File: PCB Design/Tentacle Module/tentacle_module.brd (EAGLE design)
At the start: 94 x 50.8 mm, 53 parts, among them IC1 5V, T1 NTD5867NL, T2 NTD5867NL, T3 NTD5867NL, T4 NTD5867NL, X3 RJ45-8X, X4 RJ45-8X

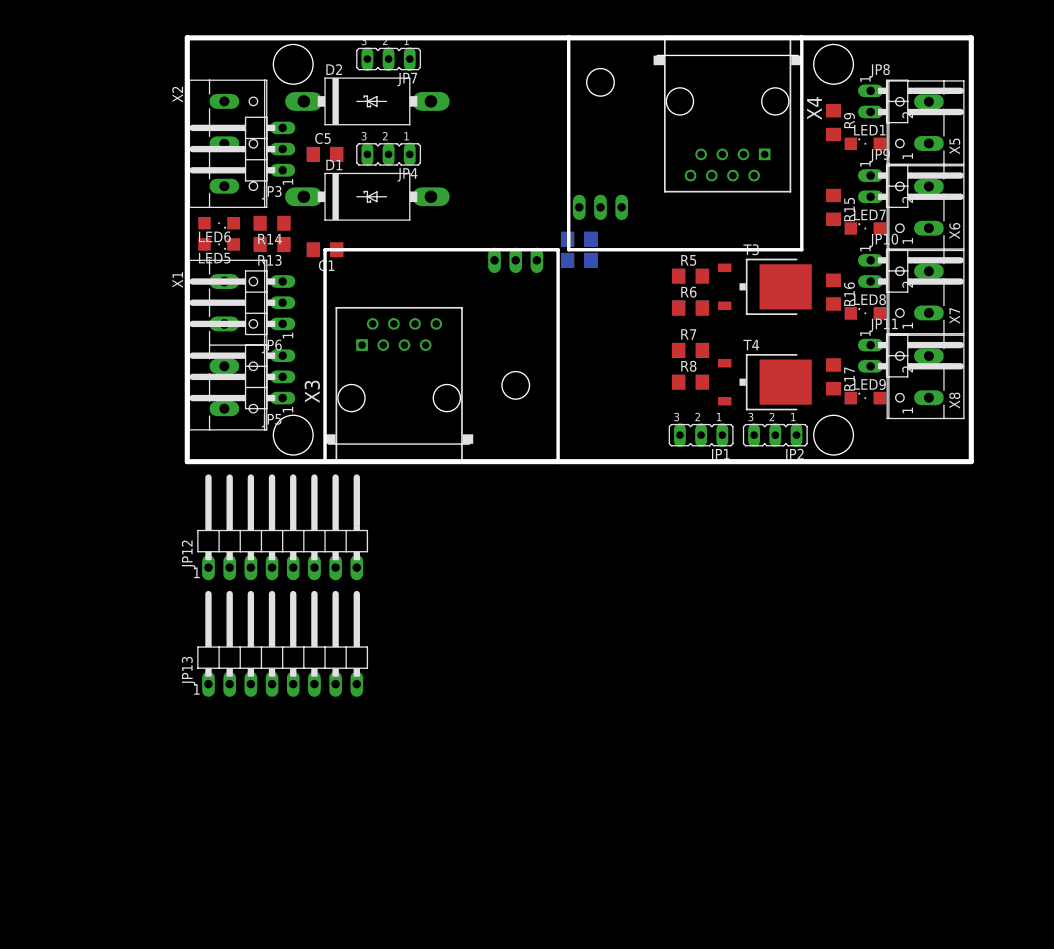
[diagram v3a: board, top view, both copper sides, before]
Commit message: Moved the location of the header
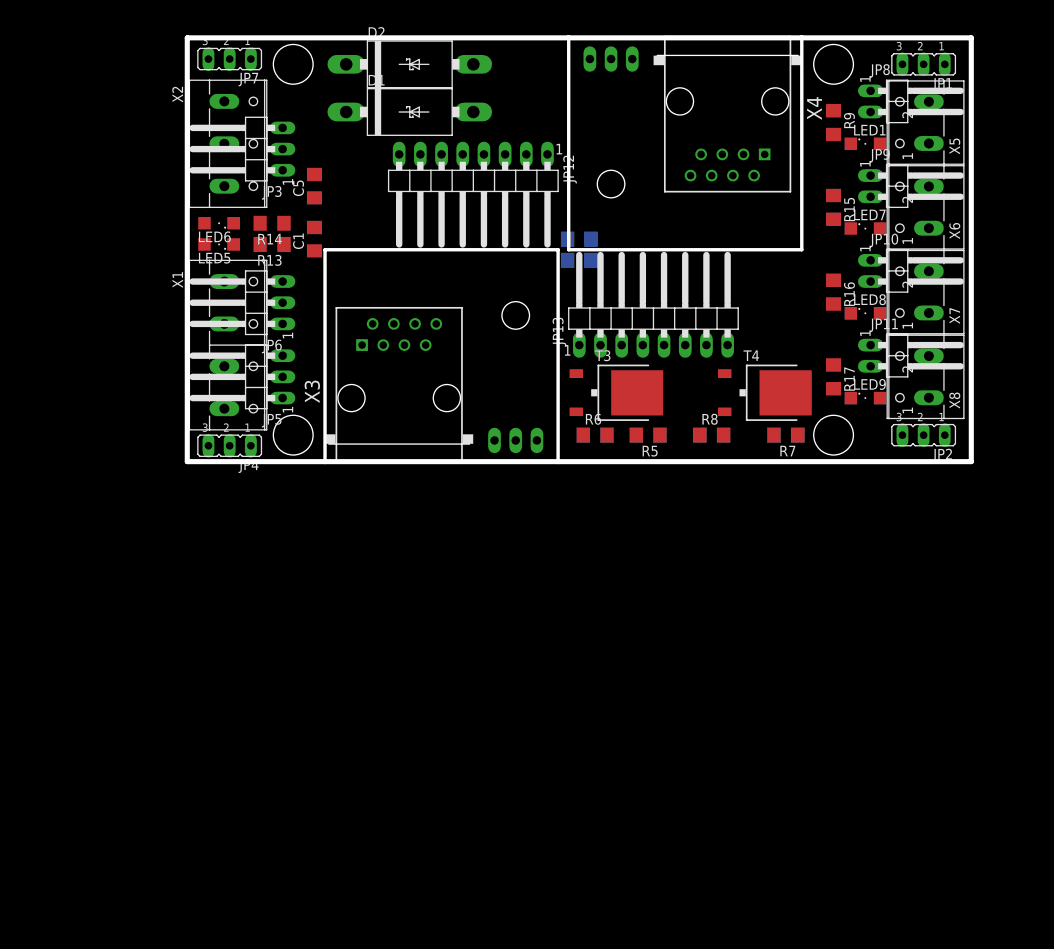
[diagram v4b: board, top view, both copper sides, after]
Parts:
- moved JP13 60.2 mm to (55.9, 17.8)
- moved JP1 51.8 mm to (88.3, 47.6)
- moved JP12 47.7 mm to (34.3, 33.0), turned to 180 degrees
- moved JP4 39.8 mm to (5.08, 1.91)
- moved R3 22.2 mm to (48.9, 3.17)
- moved T1 21.8 mm to (51.4, 8.26)
- moved T3 21.8 mm to (51.4, 8.26)
- moved R5 19.7 mm to (55.2, 3.17), turned to 180 degrees
- moved JP7 19.0 mm to (5.08, 48.3)
- moved R6 19.0 mm to (48.9, 3.17)
- moved JP2 17.8 mm to (88.3, 3.17)
- moved R1 16.1 mm to (55.2, 3.17)
- moved R7 15.3 mm to (71.8, 3.17), turned to 180 degrees
- moved IC1 14.0 mm to (39.4, 6.35), turned to 0 degrees
- moved R2 13.1 mm to (71.8, 3.17)
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
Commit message: Updated the Tentacle module schematic
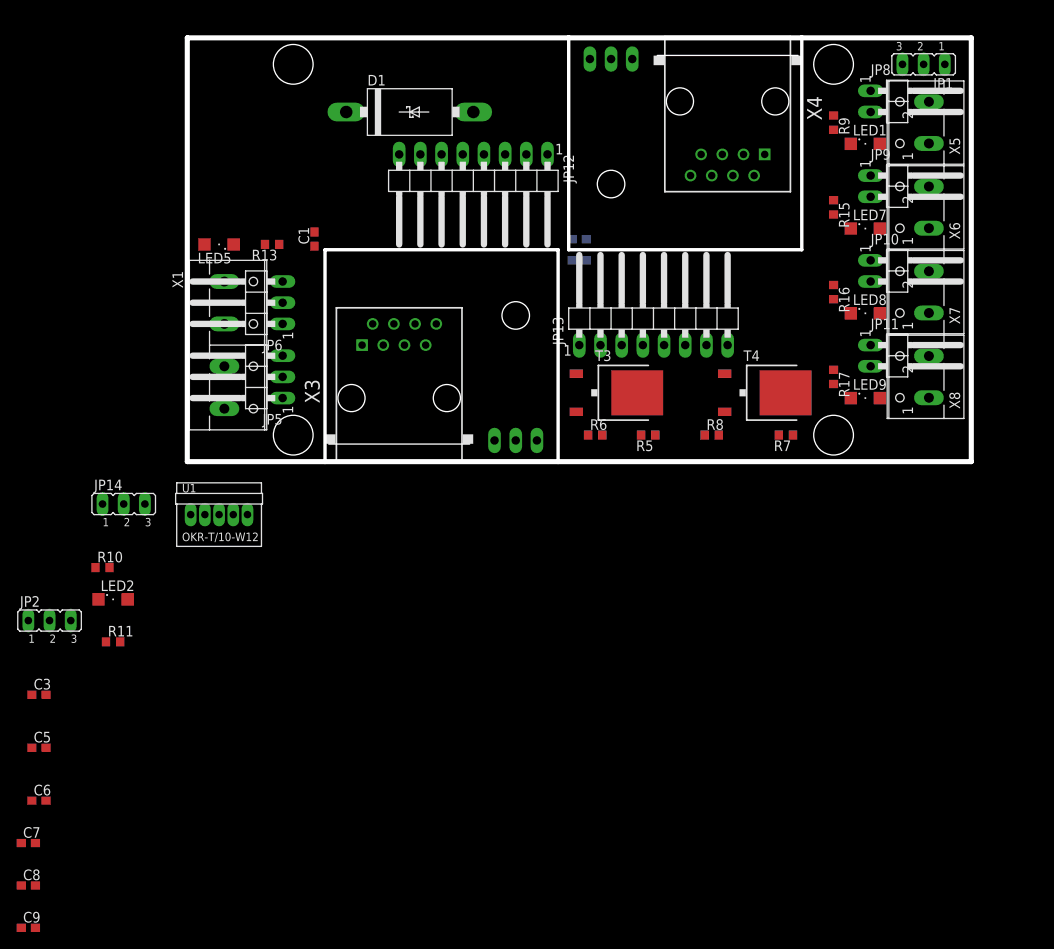
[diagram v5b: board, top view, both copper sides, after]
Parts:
- removed D2: SB540E-G, CBLA_Test_bed_Library:DO201T15
- removed JP3: (no value), CBLA_Test_bed_Library:1X03/90
- removed JP4, JP7: (no value), jumper:JP2
- removed LED6: (no value), led:SML1206
- removed R14: 470, rcl:R1206
- removed X2: (no value), con-wago-508:W237-133
- added C3, C6, C7, C8, C9: 100nF, rcl:C0603
- added JP14: (no value), jumper:JP2
- added LED2: (no value), led:SML1206
- added R10: 267, CBLA_Test_bed_Library:R0603
- added R11: 470, CBLA_Test_bed_Library:R0603
- added U1: OKR-T/10-W12, CBLA_Test_bed_Library:OKR-C90
- C1, C2, C4: device rcl:C1206 -> rcl:C0603
- C5: value 10uF -> 100nF; device rcl:C1206 -> rcl:C0603
- R1, R13, R15, R16, R17, R2, R3, R4, R5, R6, R7, R8, R9: device rcl:R1206 -> CBLA_Test_bed_Library:R0603
- moved JP2 107.1 mm to (-16.5, -19.1), turned to 0 degrees
- moved C5 75.0 mm to (-17.8, -34.3), turned to 0 degrees
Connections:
- removed net +12V1: JP7.2
- removed net +5V_SW-REG: C5.1, D2.C, JP3.1, JP3.3, X2.1, X2.3
- removed net GND1: R14.1
- removed net N$11: JP4.3, LED5.A
- removed net N$12: LED6.C, R14.2
- removed net N$13: JP7.3, LED6.A
- new net 5V_ENABLE: JP14.2, U1.ON/OFF
- new net N$6: R10.2, U1.TRIM
- new net N$7: LED2.C, R11.2
- new net PWR_LED_GND: D1.A, JP2.1, R11.1, R13.1, X1.2
- net +12V: now also JP14.3, LED5.A, U1.VIN, X1.4; no longer JP4.2
- net +3V3: now also C5.1
- net +5V: now also C3.1; no longer JP2.1, JP2.3
- net +5V_HI-PWR: now also C6.1, C7.1, C8.1, C9.1, LED2.A, U1.VOUT; no longer JP2.2
- net GND: now also C3.2, C6.2, C7.2, C8.2, C9.2, JP14.1, JP2.2, R10.1, U1.GND; no longer D1.A, D2.A, JP3.2, R13.1, X1.2, X2.2

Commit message: Preliminary part placement for the tentacle board
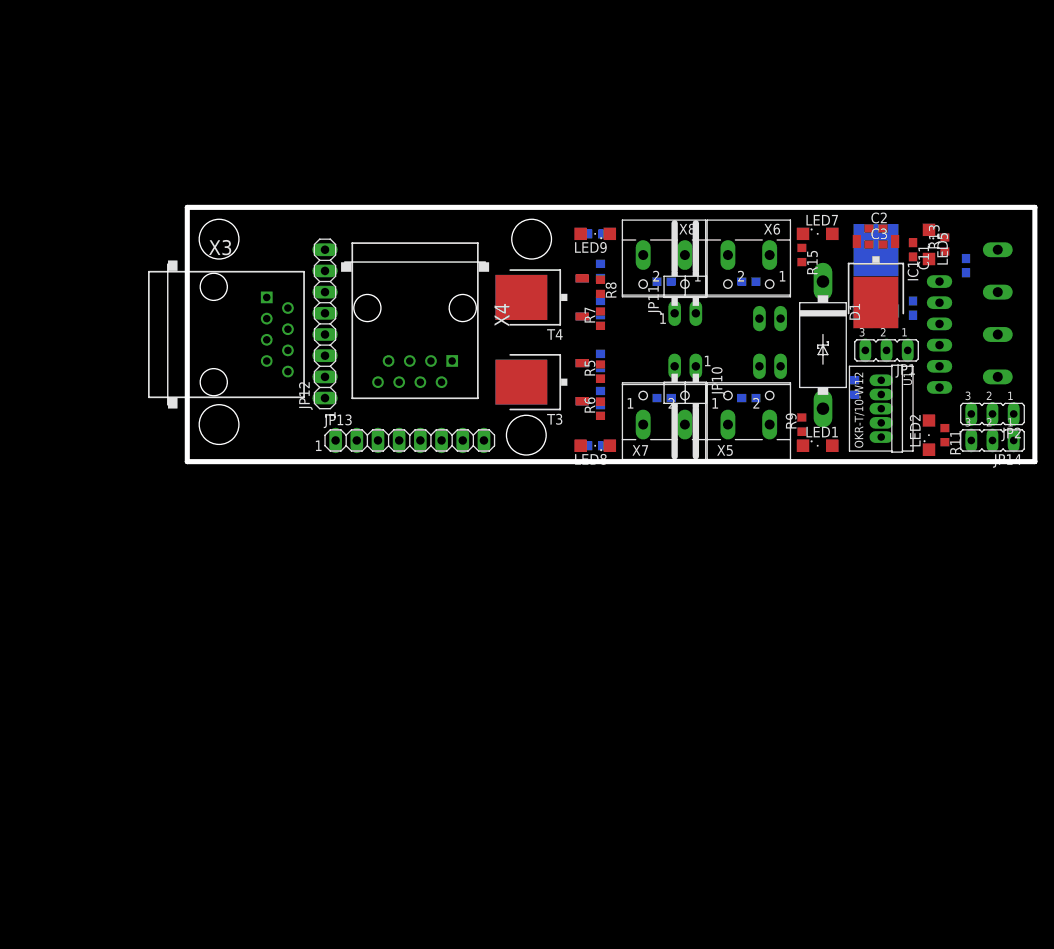
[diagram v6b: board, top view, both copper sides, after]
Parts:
- removed IC2: (no value), CBLA_Test_bed_Library:TO220L1
- added C10, C11: 10uF, rcl:C0603
- added IC3: 3.3V, CBLA_Test_bed_Library:DPACK
- IC1: value 5V -> 5.0V; device CBLA_Test_bed_Library:TO220L1 -> CBLA_Test_bed_Library:DPACK
- JP12, JP13: device CBLA_Test_bed_Library:1X08/90 -> CBLA_Test_bed_Library:1X08
- moved JP2 115.7 mm to (96.5, 5.71), turned to 180 degrees
- moved C3 113.9 mm to (82.5, 26.0)
- moved C5 113.3 mm to (82.5, 18.4), flipped to the bottom, turned to 180 degrees
- moved C7 109.5 mm to (67.3, 21.6), flipped to the bottom, turned to 180 degrees
- moved C9 108.7 mm to (57.1, 21.6), flipped to the bottom, turned to 180 degrees
- moved JP14 104.4 mm to (96.5, 2.54), turned to 180 degrees
- moved R11 102.7 mm to (90.8, 3.17), turned to 270 degrees
- moved LED2 99.8 mm to (88.9, 3.17), turned to 90 degrees
- moved C6 97.8 mm to (67.3, 7.62), flipped to the bottom
- moved C8 96.0 mm to (57.1, 7.62), flipped to the bottom
- moved R10 92.7 mm to (80.0, 8.89), flipped to the bottom, turned to 270 degrees
- moved X1 91.5 mm to (96.5, 17.8), flipped to the bottom
- moved JP5 86.8 mm to (94.0, 19.1), flipped to the bottom
- moved JP6 86.7 mm to (94.0, 11.4), flipped to the bottom
- moved LED5 85.1 mm to (88.9, 26.0), turned to 270 degrees
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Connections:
- removed net N$15: LED8.C, R16.2
- removed net N$16: LED9.C, R17.2
- new net N$12: LED7.A, R15.1
- new net N$13: LED8.A, R16.1
- net +12V: now also C10.1, C11.1, IC3.1; no longer IC2.1
- net +3V3: now also IC3.3; no longer IC2.3
- net +5V: no longer JP1.2
- net +5V_HI-PWR: now also JP1.2
- net GND: now also C10.2, C11.2, IC3.2; no longer IC2.2
- net N$14: now also LED9.A, R17.1; no longer LED7.C, R15.2
- net N$5: now also LED1.A, R9.1; no longer LED1.C, R9.2
- net PWR_LED_GND: now also JP2.3; no longer JP2.1
- net SMA1_OUT-: now also LED1.C; no longer R9.1
- net SMA2_OUT-: now also LED7.C; no longer R15.1
- net SMA3_OUT-: now also LED8.C; no longer R16.1
- net SMA4_OUT-: now also LED9.C; no longer R17.1
- net TEST_LED_V+: now also R15.2, R16.2, R17.2, R9.2; no longer LED1.A, LED7.A, LED8.A, LED9.A
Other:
- board size 94 x 50.8 mm -> 101.6 x 30.5 mm

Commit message: Finished routing the Tentacle module board
Not changing it!
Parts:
- added JP3: (no value), CBLA_Test_bed_Library:1X03/90
- moved R3 13.1 mm to (37.5, 12.7)
- moved R6 13.1 mm to (37.5, 11.4), turned to 270 degrees
- moved R1 12.5 mm to (37.5, 8.89), turned to 90 degrees
- moved R5 12.5 mm to (37.5, 7.62)
- moved R4 12.2 mm to (37.5, 21.0)
- moved R2 12.1 mm to (37.5, 17.1)
- moved R7 12.1 mm to (37.5, 17.1)
- moved R8 12.1 mm to (37.5, 21.0)
- moved C11 3.81 mm to (87.0, 21.6)
- moved C8 3.17 mm to (54.0, 7.62)
- moved T1 2.84 mm to (45.1, 10.8), turned to 90 degrees
- moved T3 2.84 mm to (45.1, 10.8), turned to 270 degrees
- moved T2 2.54 mm to (45.1, 19.7), turned to 90 degrees
- moved T4 2.54 mm to (45.1, 19.7), turned to 270 degrees
- moved C9 2.01 mm to (59.1, 22.2)
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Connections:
- removed net +3V3: C4.1, C5.1, IC3.3
- net +3.3V: now also C4.1, C5.1, IC3.3
- net +5V: now also JP3.2
- net GND: now also D1.A, JP3.3, X1.2
- net IR1: now also JP3.1
- net PWR_LED_GND: no longer D1.A, X1.2
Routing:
- net +5V: track 0.00 -> 99.9 mm, vias 0 -> 1
- net +5V_HI-PWR: track 0.00 -> 99.8 mm
- net +12V: track 0.00 -> 94.0 mm
- net TEST_LED_V+: track 0.00 -> 93.4 mm, vias 0 -> 2
- net +3.3V: track 0.00 -> 69.9 mm, vias 0 -> 1
- net IR1: track 0.00 -> 52.7 mm
- net SMA2_OUT-: track 0.00 -> 48.4 mm
- net PWM2: track 0.00 -> 43.5 mm
- net SCL: track 0.00 -> 37.5 mm
- net PWM3: track 0.00 -> 37.4 mm
- net SMA1_OUT-: track 0.00 -> 36.5 mm, vias 0 -> 1
- net PWM1: track 0.00 -> 36.0 mm
- net SDA: track 0.00 -> 35.0 mm
- net PWM4: track 0.00 -> 32.0 mm, vias 0 -> 1
- net SMA4_OUT-: track 0.00 -> 29.1 mm
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- added copper zone on layer 1, net GND
- added copper zone on layer 16, net GND

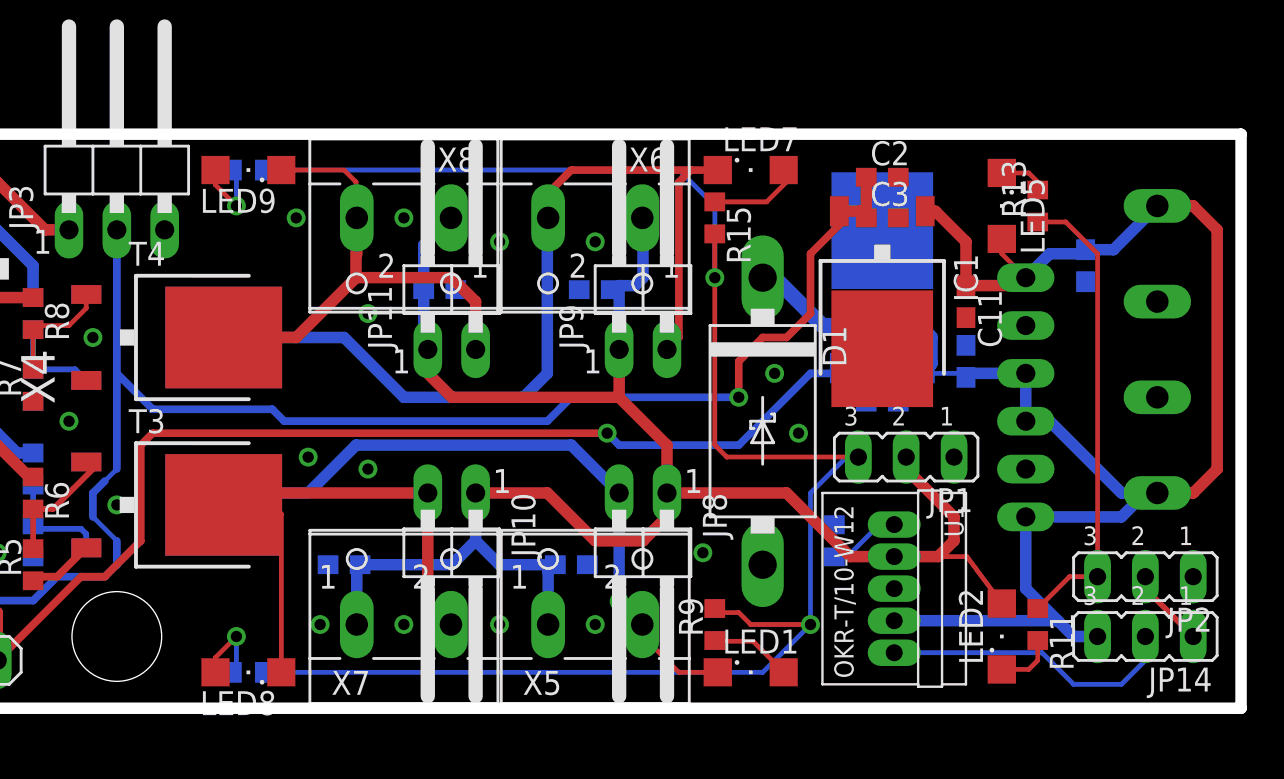
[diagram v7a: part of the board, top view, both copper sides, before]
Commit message: made modifications to board design and correct errors
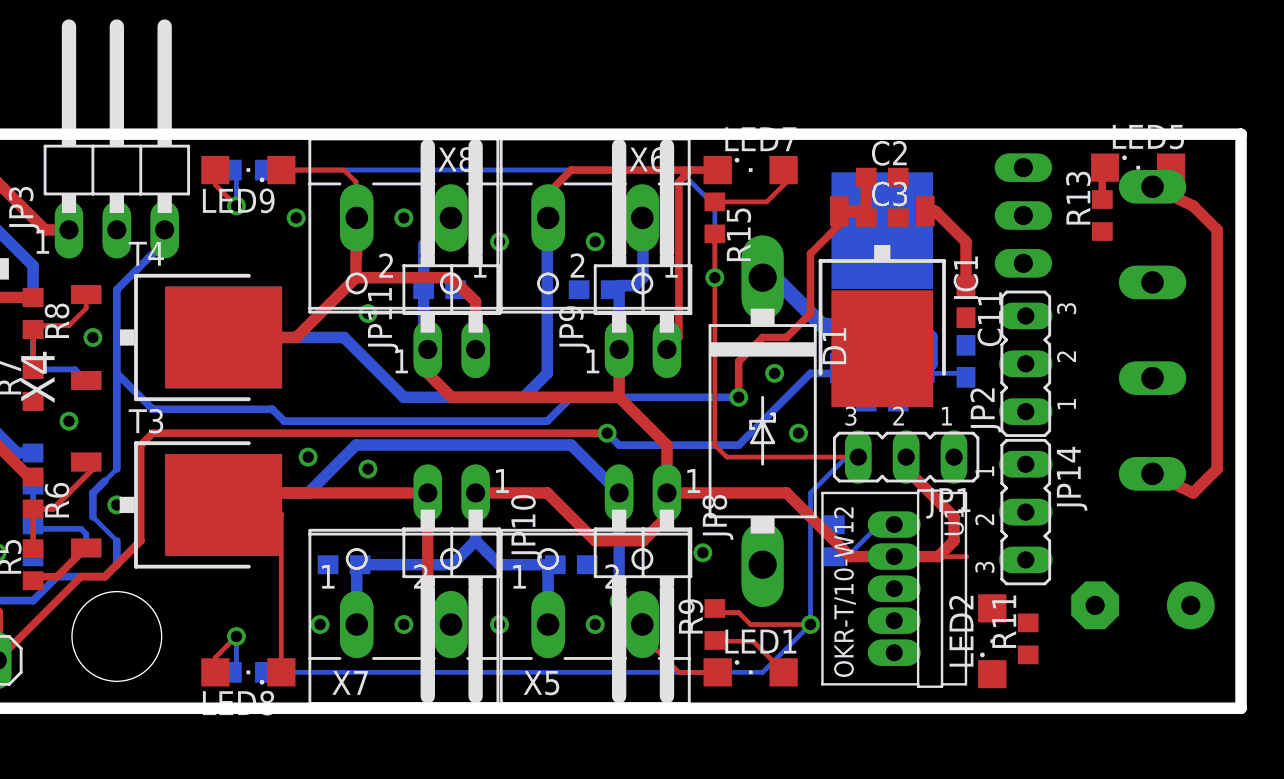
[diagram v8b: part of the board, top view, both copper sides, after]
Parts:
- removed JP5: (no value), CBLA_Test_bed_Library:1X03/90
- C1: device rcl:C0603 -> rcl:E5-10,5
- moved C1 18.3 mm to (96.4, 5.46), turned to 0 degrees
- moved JP6 13.5 mm to (93.9, 26.2)
- moved JP2 13.0 mm to (90.2, 18.3), turned to 90 degrees
- moved JP14 9.16 mm to (90.2, 10.4), turned to 270 degrees
- moved LED5 7.52 mm to (96.1, 28.7), turned to 0 degrees
- moved R13 3.47 mm to (94.2, 26.2)
- moved X1 1.05 mm to (96.3, 20.1)
- moved R11 0.92 mm to (90.3, 3.68), turned to 90 degrees
- moved LED2 0.57 mm to (88.4, 3.56)
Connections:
- net +12V: now also C1.+; no longer C1.1, JP5.1, JP5.3
- net +5V: now also JP3.3; no longer JP3.2
- net GND: now also C1.-, JP3.2; no longer C1.2, JP3.3, JP5.2
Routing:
- net +12V: track 94.0 -> 43.5 mm
- net PWR_LED_GND: track 24.9 -> 0.32 mm
- net 5V_ENABLE: track 15.8 -> 0.00 mm
- net GND: track 7.77 -> 3.54 mm
- net N$7: track 3.16 -> 0.00 mm
- net +5V_HI-PWR: track 99.8 -> 96.7 mm
- net +5V: track 99.9 -> 101.0 mm
- net N$10: track 2.52 -> 1.75 mm
